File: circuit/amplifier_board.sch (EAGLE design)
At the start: 17 parts

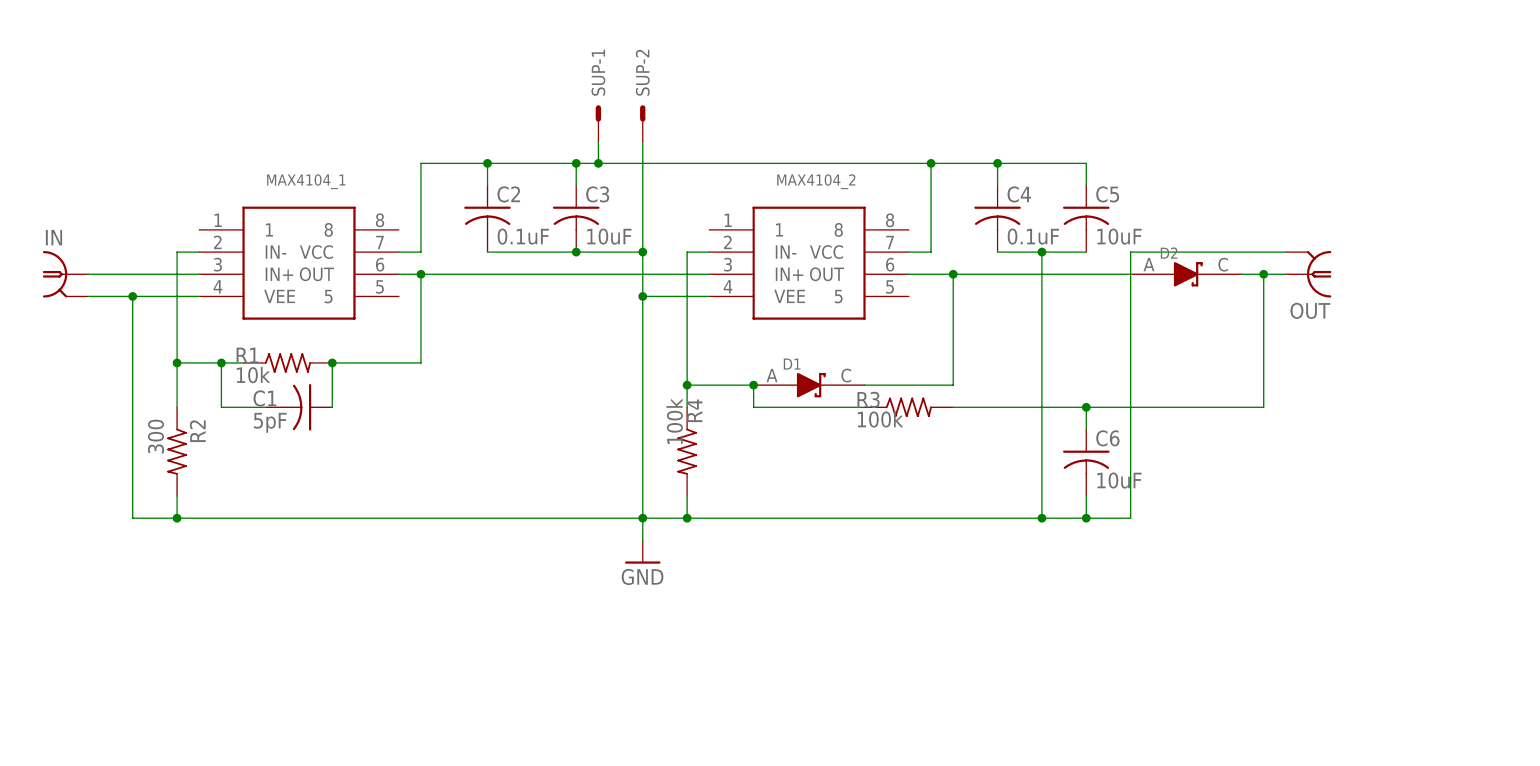
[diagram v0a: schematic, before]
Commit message: boards: Changed components to be correct; increased board size to be solderable.
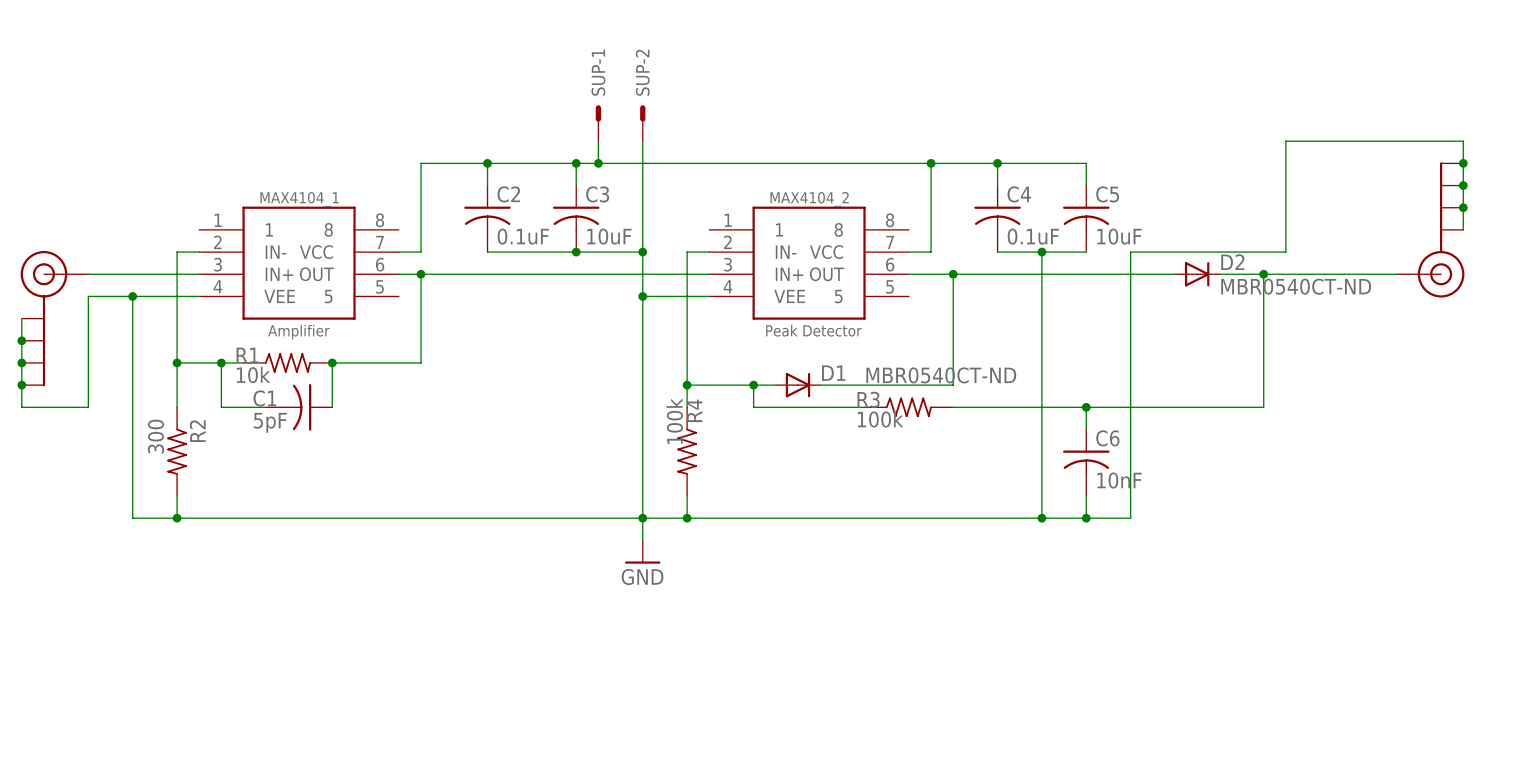
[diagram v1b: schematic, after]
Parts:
- C6: value 10uF -> 10nF
- D1, D2: value (none) -> MBR0540CT-ND; device 000phys605parts:SCH_D1 -> diode:CGRM4001-G
- IN, OUT: value LTI-SASF54GT -> SMA_EDGE; device con-coax:LTI-SASF54GT -> SparkFun-Retired:SMA_EDGE
- MAX4104_1: value (none) -> Amplifier
- MAX4104_2: value (none) -> Peak Detector
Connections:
- net DIG_READOUT: now also D2.C, OUT.SIGNAL; no longer D2.OUT, OUT.1
- net GND: now also IN.GND@0, IN.GND@1, IN.GND@2, IN.GND@3, OUT.GND@0, OUT.GND@1, OUT.GND@2, OUT.GND@3; no longer IN.2, OUT.2
- net IN: now also IN.SIGNAL; no longer IN.1
- net IN-_2: now also D1.A; no longer D1.IN
- net OUT_2: now also D1.C, D2.A; no longer D1.OUT, D2.IN

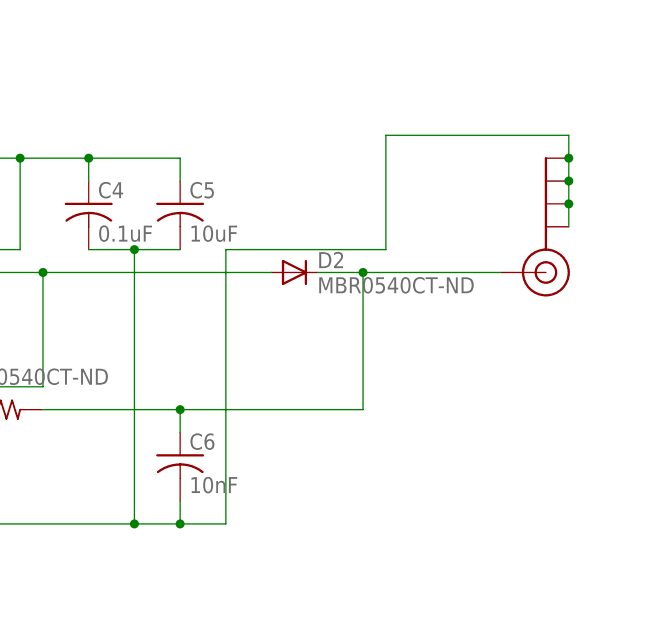
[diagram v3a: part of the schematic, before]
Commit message: boards: Changes to library and board designs.
Will I need to remove the vias and replace them with holes in order to be able to ground both sides?
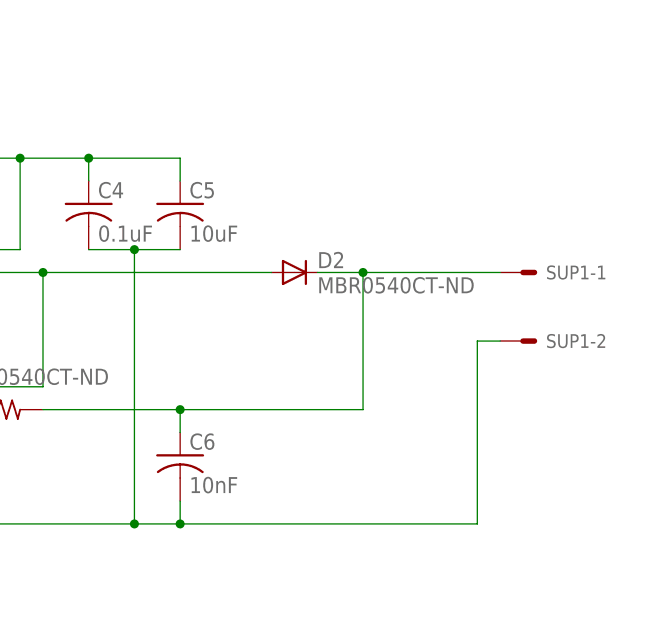
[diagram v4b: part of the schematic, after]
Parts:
- removed OUT: SMA_EDGE, SparkFun-Retired:SMA_EDGE
- added SUP1: 332-02, con-garry:332-02
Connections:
- net DIG_READOUT: now also SUP1-1.S; no longer OUT.SIGNAL
- net GND: now also SUP1-2.S; no longer OUT.GND@0, OUT.GND@1, OUT.GND@2, OUT.GND@3
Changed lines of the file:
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@@
 <clearance class="0" value="0.3048"/>
 </class>
-<class number="1" name="high_freq" width="0.184303125" drill="0">
+<class number="1" name="high_freq" width="3.021" drill="0">
 <clearance class="0" value="0.508"/>
 <clearance class="1" value="0.508"/>
@@
 <part name="R4" library="rcl" library_urn="urn:adsk.eagle:library:334" deviceset="R-US_" device="M0805" package3d_urn="urn:adsk.eagle:package:23556/1" value="100k"/>
 <part name="C6" library="rcl" library_urn="urn:adsk.eagle:library:334" deviceset="C-US" device="C0805" package3d_urn="urn:adsk.eagle:package:23617/2" value="10nF"/>
-<part name="OUT" library="SparkFun-Retired" deviceset="SMA_EDGE" device=""/>
 <part name="IN" library="SparkFun-Retired" deviceset="SMA_EDGE" device=""/>
 <part name="D1" library="diode" library_urn="urn:adsk.eagle:library:210" deviceset="CGRM400*-G" device="" package3d_urn="urn:adsk.eagle:package:43457/2" technology="1" value="MBR0540CT-ND"/>
 <part name="D2" library="diode" library_urn="urn:adsk.eagle:library:210" deviceset="CGRM400*-G" device="" package3d_urn="urn:adsk.eagle:package:43457/2" technology="1" value="MBR0540CT-ND"/>
+<part name="SUP1" library="con-garry" library_urn="urn:adsk.eagle:library:147" deviceset="332-02" device="" package3d_urn="urn:adsk.eagle:package:6810/1"/>
 </parts>
 <sheets>
@@
 </instance>
 <instance part="C6" gate="G$1" x="160.02" y="30.48"/>
-<instance part="OUT" gate="1" x="200.66" y="50.8" rot="R180"/>
 <instance part="IN" gate="1" x="40.64" y="50.8"/>
 <instance part="D1" gate="G$1" x="127" y="38.1" smashed="yes">
@@
 </instance>
 <instance part="D2" gate="G$1" x="172.72" y="50.8"/>
+<instance part="SUP1" gate="-1" x="198.12" y="50.8" smashed="yes">
+<attribute name="NAME" x="200.66" y="50.038" size="1.524" layer="95"/>
+</instance>
+<instance part="SUP1" gate="-2" x="198.12" y="43.18" smashed="yes">
+<attribute name="NAME" x="200.66" y="42.418" size="1.524" layer="95"/>
+</instance>
 </instances>
 <busses>
 </busses>
 <nets>
-<net name="AMP" class="1">
+<net name="AMP" class="0">
 <segment>
 <pinref part="R1" gate="G$1" pin="2"/>
@@
 </segment>
 </net>
-<net name="IN-_1" class="1">
+<net name="IN-_1" class="0">
 <segment>
 <pinref part="C1" gate="G$1" pin="2"/>
@@
 <wire x1="45.72" y1="48.26" x2="50.8" y2="48.26" width="0.1524" layer="91"/>
 <junction x="50.8" y="48.26"/>
-<wire x1="182.88" y1="53.34" x2="165.1" y2="53.34" width="0.1524" layer="91"/>
-<wire x1="165.1" y1="53.34" x2="165.1" y2="22.86" width="0.1524" layer="91"/>
-<wire x1="165.1" y1="22.86" x2="160.02" y2="22.86" width="0.1524" layer="91"/>
 <junction x="160.02" y="22.86"/>
 <wire x1="45.72" y1="48.26" x2="45.72" y2="35.56" width="0.1524" layer="91"/>
@@
 <wire x1="38.1" y1="43.18" x2="38.1" y2="45.72" width="0.1524" layer="91"/>
 <junction x="38.1" y="43.18"/>
-<wire x1="182.88" y1="53.34" x2="182.88" y2="66.04" width="0.1524" layer="91"/>
-<wire x1="182.88" y1="66.04" x2="203.2" y2="66.04" width="0.1524" layer="91"/>
-<pinref part="OUT" gate="1" pin="GND@0"/>
-<pinref part="OUT" gate="1" pin="GND@1"/>
-<pinref part="OUT" gate="1" pin="GND@2"/>
-<pinref part="OUT" gate="1" pin="GND@3"/>
-<wire x1="203.2" y1="63.5" x2="203.2" y2="60.96" width="0.1524" layer="91"/>
-<junction x="203.2" y="60.96"/>
-<wire x1="203.2" y1="60.96" x2="203.2" y2="58.42" width="0.1524" layer="91"/>
-<junction x="203.2" y="58.42"/>
-<wire x1="203.2" y1="58.42" x2="203.2" y2="55.88" width="0.1524" layer="91"/>
-<wire x1="203.2" y1="66.04" x2="203.2" y2="63.5" width="0.1524" layer="91"/>
-<junction x="203.2" y="63.5"/>
-</segment>
-</net>
-<net name="DIG_READOUT" class="1">
+<wire x1="160.02" y1="22.86" x2="193.04" y2="22.86" width="0.1524" layer="91"/>
+<wire x1="193.04" y1="22.86" x2="193.04" y2="43.18" width="0.1524" layer="91"/>
+<pinref part="SUP1" gate="-2" pin="S"/>
+<wire x1="193.04" y1="43.18" x2="195.58" y2="43.18" width="0.1524" layer="91"/>
+</segment>
+</net>
+<net name="DIG_READOUT" class="0">
 <segment>
 <wire x1="180.34" y1="35.56" x2="180.34" y2="50.8" width="0.1524" layer="91"/>
@@
 <wire x1="180.34" y1="50.8" x2="195.58" y2="50.8" width="0.1524" layer="91"/>
 <junction x="180.34" y="50.8"/>
-<pinref part="OUT" gate="1" pin="SIGNAL"/>
 <pinref part="D2" gate="G$1" pin="C"/>
 <wire x1="175.26" y1="50.8" x2="180.34" y2="50.8" width="0.1524" layer="91"/>
-</segment>
-</net>
-<net name="OUT_2" class="1">
+<pinref part="SUP1" gate="-1" pin="S"/>
+</segment>
+</net>
+<net name="OUT_2" class="0">
 <segment>
 <wire x1="129.54" y1="38.1" x2="144.78" y2="38.1" width="0.1524" layer="91"/>
@@
 </segment>
 </net>
-<net name="IN-_2" class="1">
+<net name="IN-_2" class="0">
 <segment>
 <pinref part="R4" gate="G$1" pin="1"/>

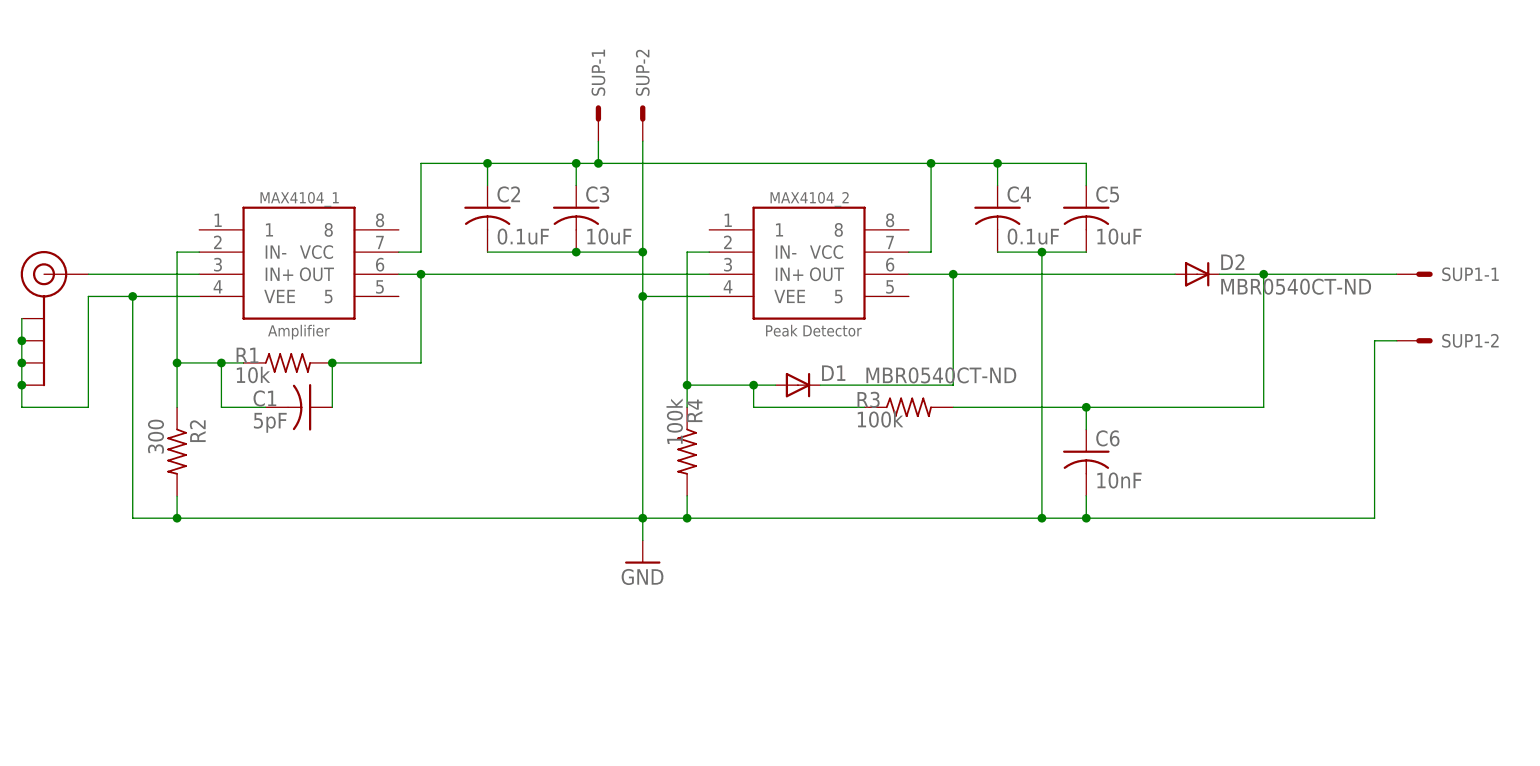
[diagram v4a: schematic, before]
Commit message: boards: Changed packages of cap and resistors to be 0603, as we will have available.  Also changed mount points to be grounded, and made vias solderable.
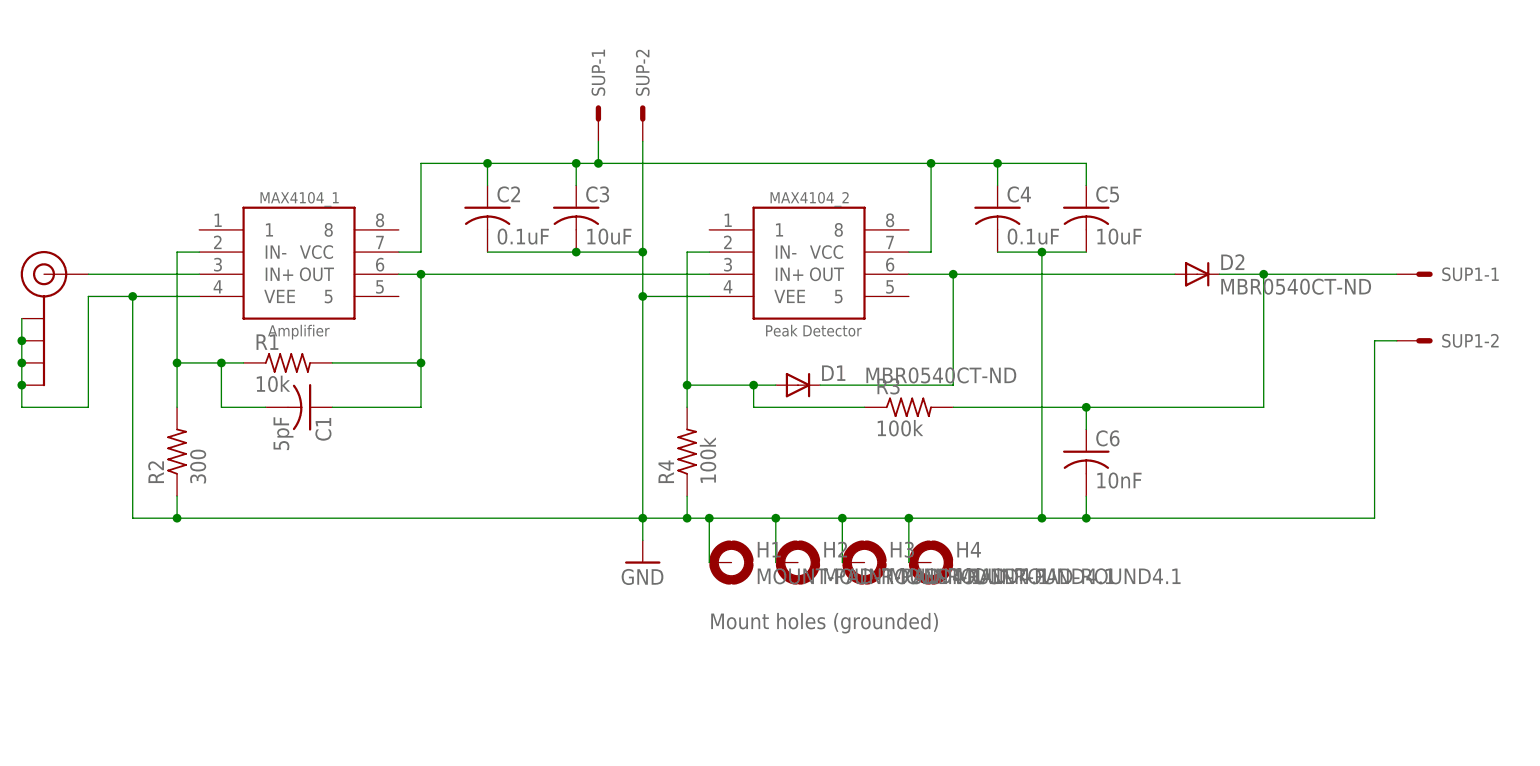
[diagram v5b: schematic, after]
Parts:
- added H1, H2, H3, H4: MOUNT-PAD-ROUND4.1, holes:MOUNT-PAD-ROUND4.1
- C1, C2, C3, C4, C5, C6: device rcl:C-USC0805 -> rcl:C-USC0603
- R1, R2, R3, R4: device rcl:R-US_M0805 -> rcl:R-US_R0603
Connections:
- net GND: now also H1.MOUNT, H2.MOUNT, H3.MOUNT, H4.MOUNT, R2.1, R4.1; no longer R2.2, R4.2
- net IN-_1: now also R2.2; no longer R2.1
- net IN-_2: now also R4.2; no longer R4.1
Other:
- note added: "Mount holes (grounded)"
- moved on the sheet: R2, R4

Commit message: Modified board. Tried to add Spice model.
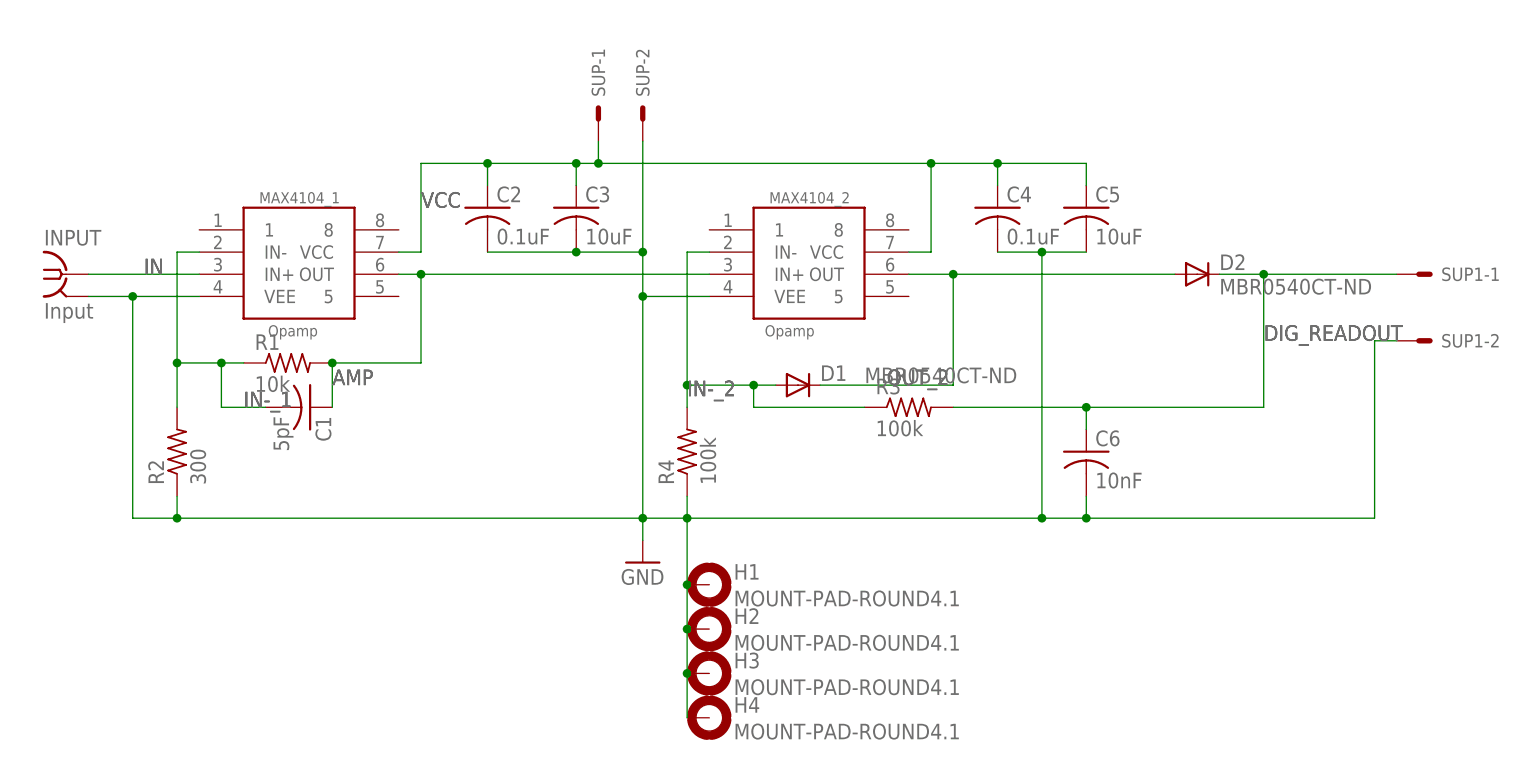
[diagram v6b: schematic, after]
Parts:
- removed IN: SMA_EDGE, SparkFun-Retired:SMA_EDGE
- added INPUT: Input, 000phys605parts:SMA-EDGE
- D1, D2: SPICEMODEL (none) -> DMBR0540; SPICEPREFIX (none) -> D
- MAX4104_1: value Amplifier -> Opamp; SPICEMODEL (none) -> MAX4104; SPICEPREFIX (none) -> X
- MAX4104_2: value Peak Detector -> Opamp; SPICEMODEL (none) -> MAX4104; SPICEPREFIX (none) -> X
- SUP: SPICEMODEL (none) -> VoltageSource; SPICEPREFIX (none) -> X
- SUP1: SPICEMODEL (none) -> TerminalOut; SPICEPREFIX (none) -> X
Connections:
- net GND: now also INPUT.2; no longer IN.GND@0, IN.GND@1, IN.GND@2, IN.GND@3
- net IN: now also INPUT.1; no longer IN.SIGNAL
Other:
- note removed: "Mount holes (grounded)"
- moved on the sheet: H1, H2, H3, H4
